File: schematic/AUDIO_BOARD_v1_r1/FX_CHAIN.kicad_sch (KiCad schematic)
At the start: 25 parts, among them U40 LM13700, U41 4053, U42 OPA1678

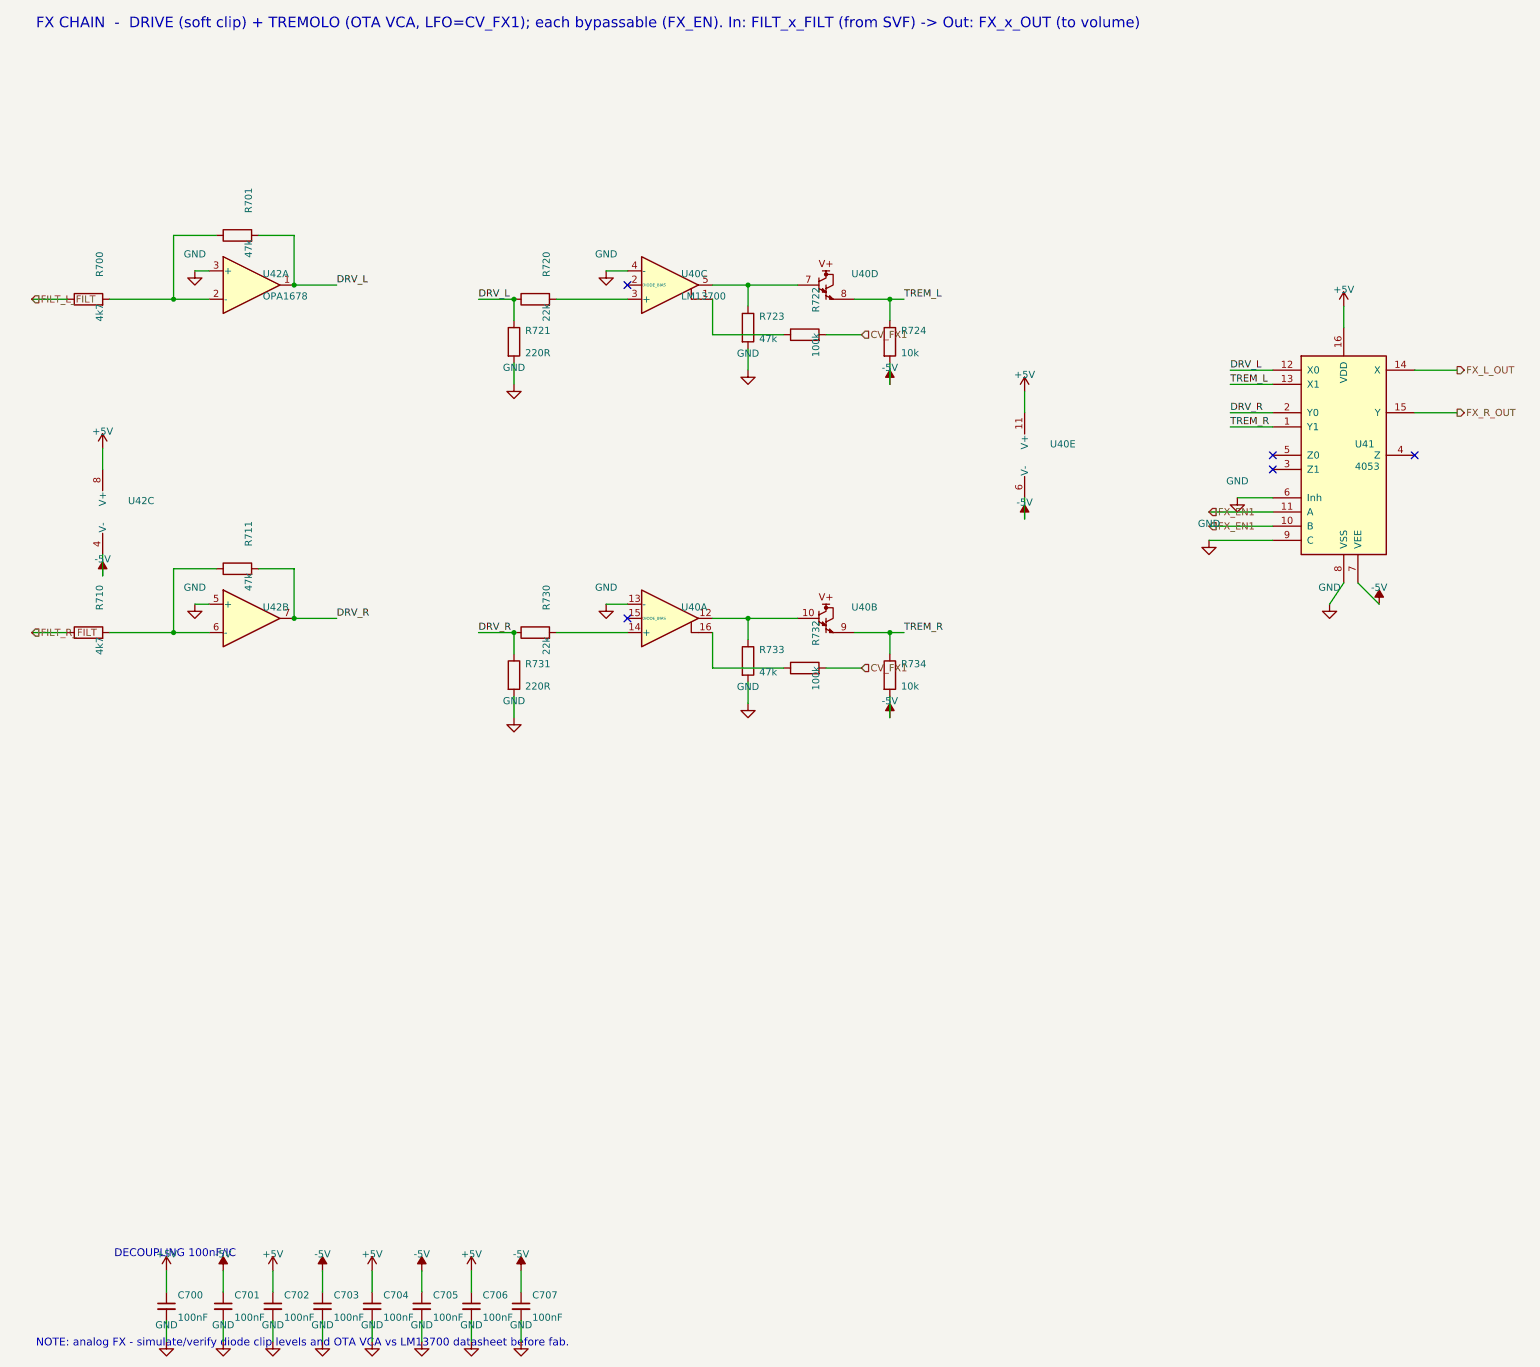
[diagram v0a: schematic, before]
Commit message: more placement and routing
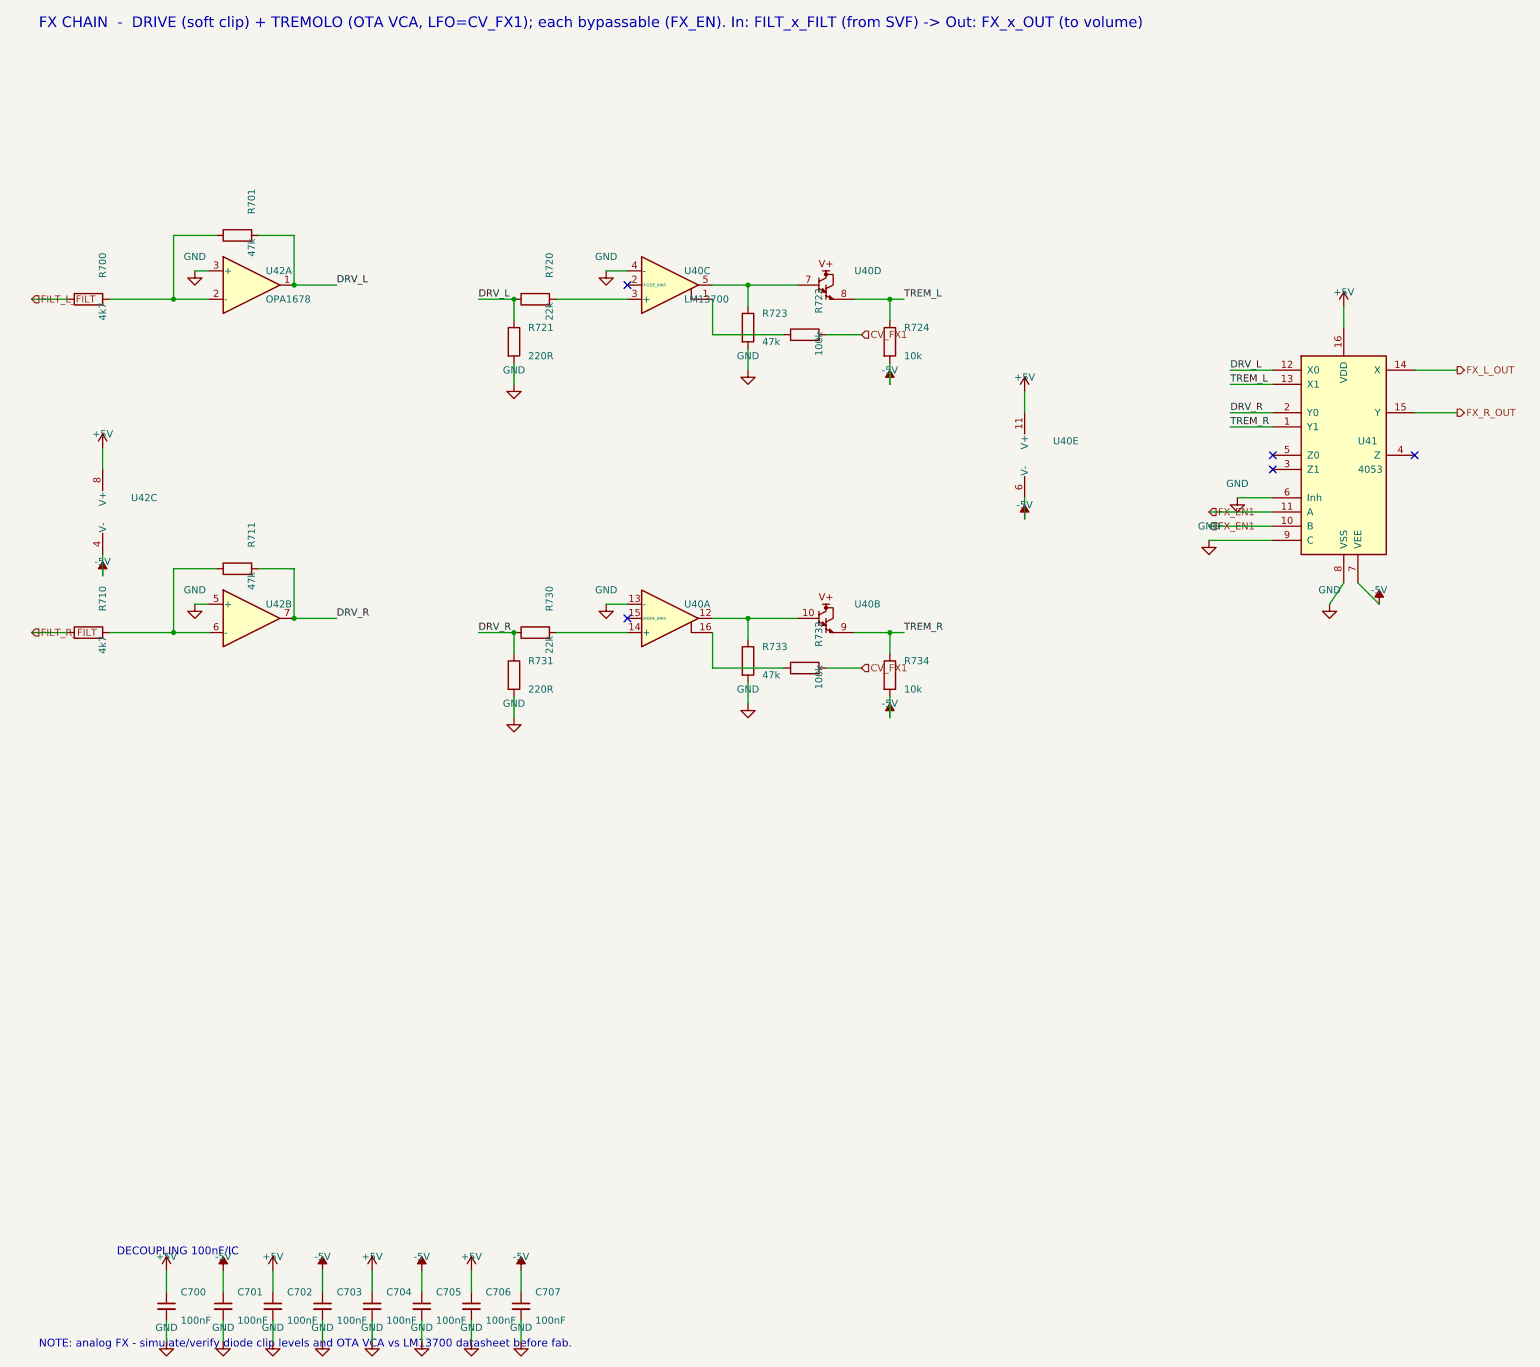
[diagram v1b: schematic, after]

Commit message: placement. start with each sheet for the most part
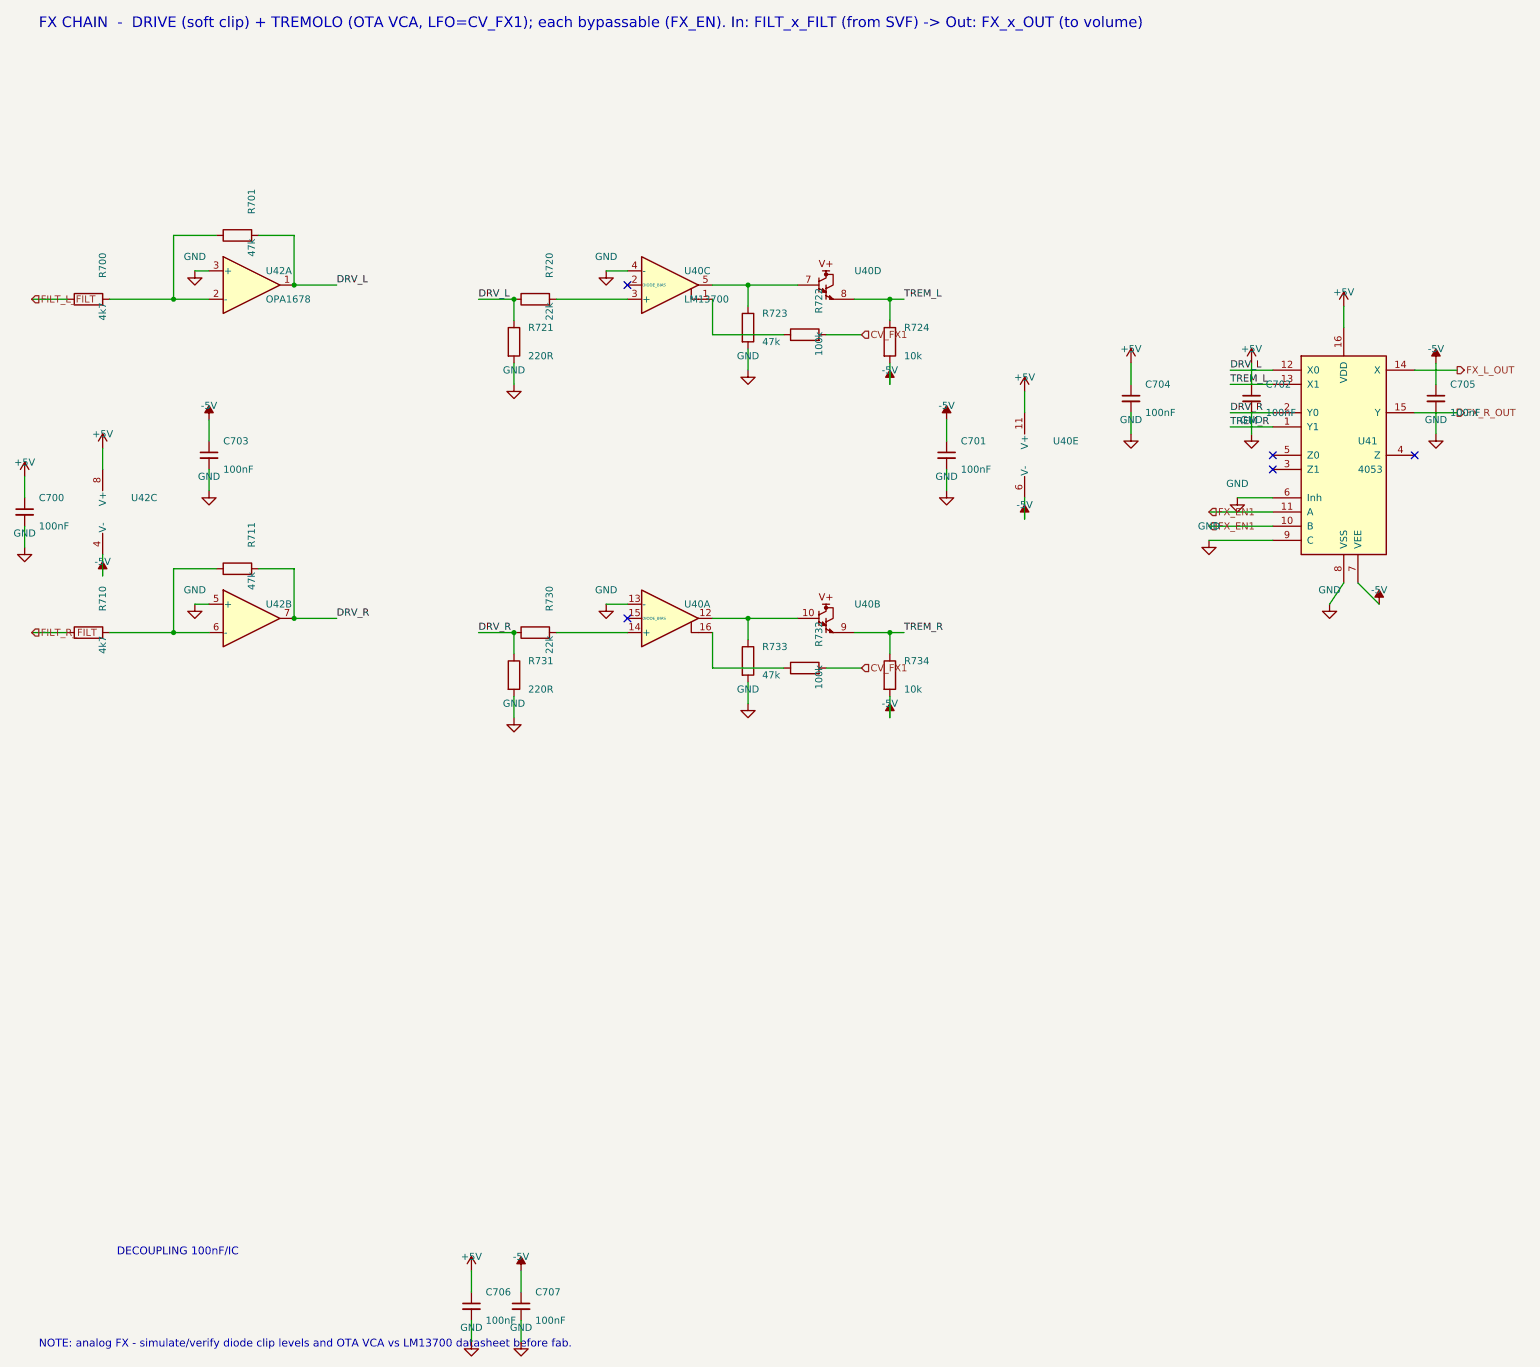
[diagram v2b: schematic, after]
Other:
- moved on the sheet: C700, C701, C702, C703, C704, C705

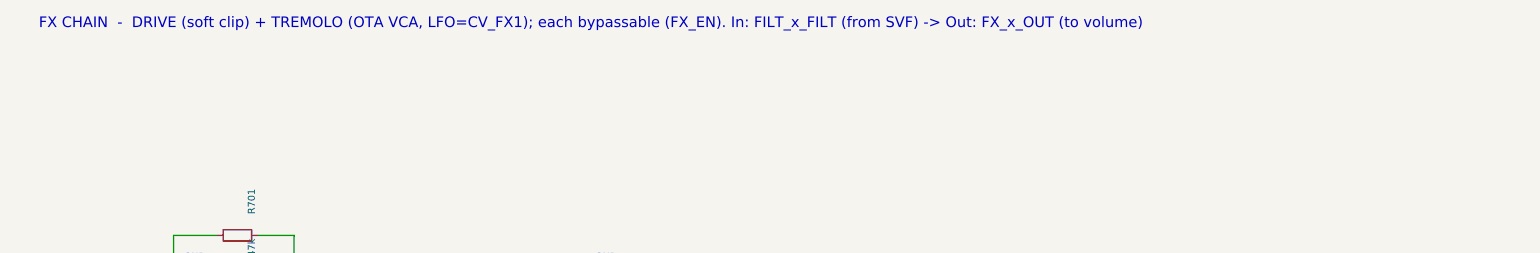
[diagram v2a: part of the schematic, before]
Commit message: more routing. more placement
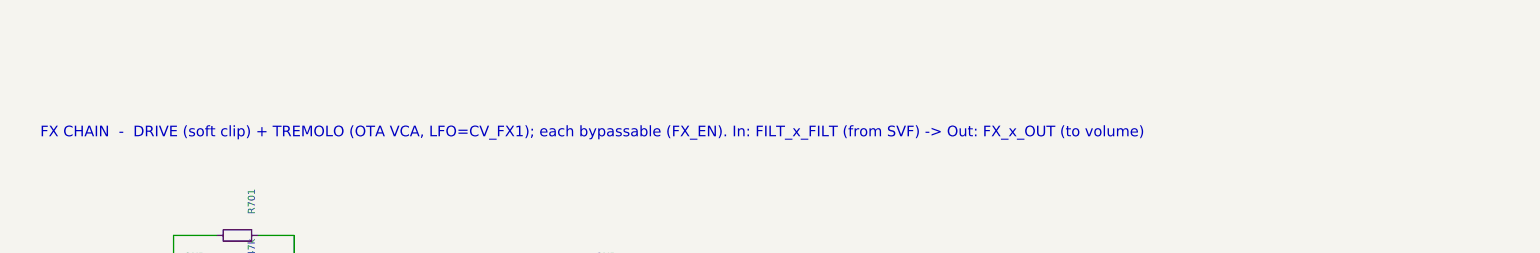
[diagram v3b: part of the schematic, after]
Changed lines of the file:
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@@
 	(text "FX CHAIN  -  DRIVE (soft clip) + TREMOLO (OTA VCA, LFO=CV_FX1); each bypassable (FX_EN). In: FILT_x_FILT (from SVF) -> Out: FX_x_OUT (to volume)"
 		(exclude_from_sim no)
-		(at 16.51 13.97 0)
+		(at 16.764 33.528 0)
 		(effects
 			(font
